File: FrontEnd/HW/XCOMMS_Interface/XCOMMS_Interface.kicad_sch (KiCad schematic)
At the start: 37 parts, among them J1 TFC-110-02-F-D-A-P-FR, J2 PicoBlade01x05, J3 PicoBlade01x05, J4 PicoBlade01x02, U1 STM32L051K8Tx, Y1 ECS-.327-7-34QCS-TR

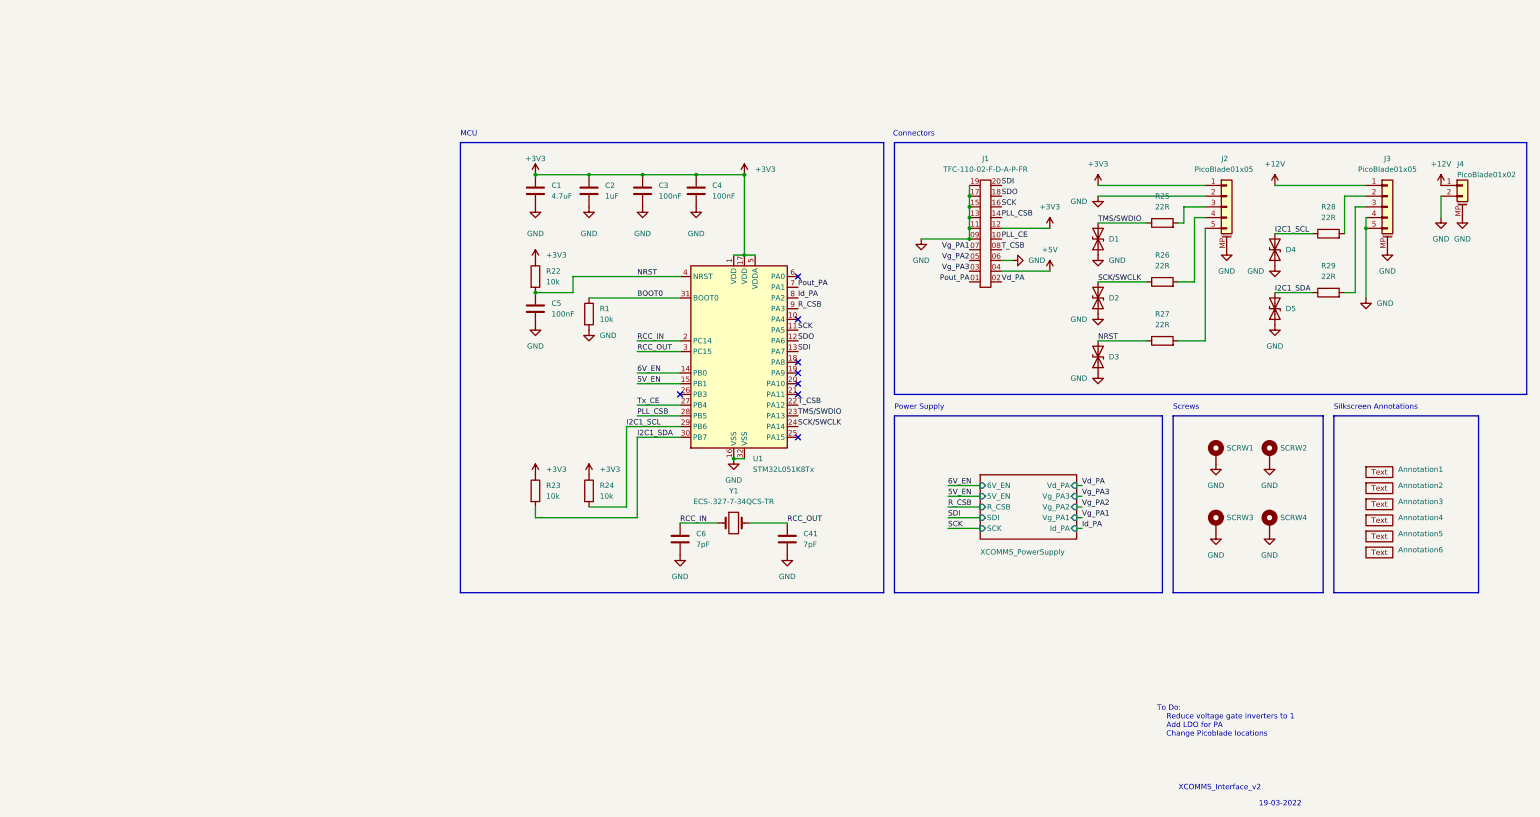
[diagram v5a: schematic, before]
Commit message: redundant MCU
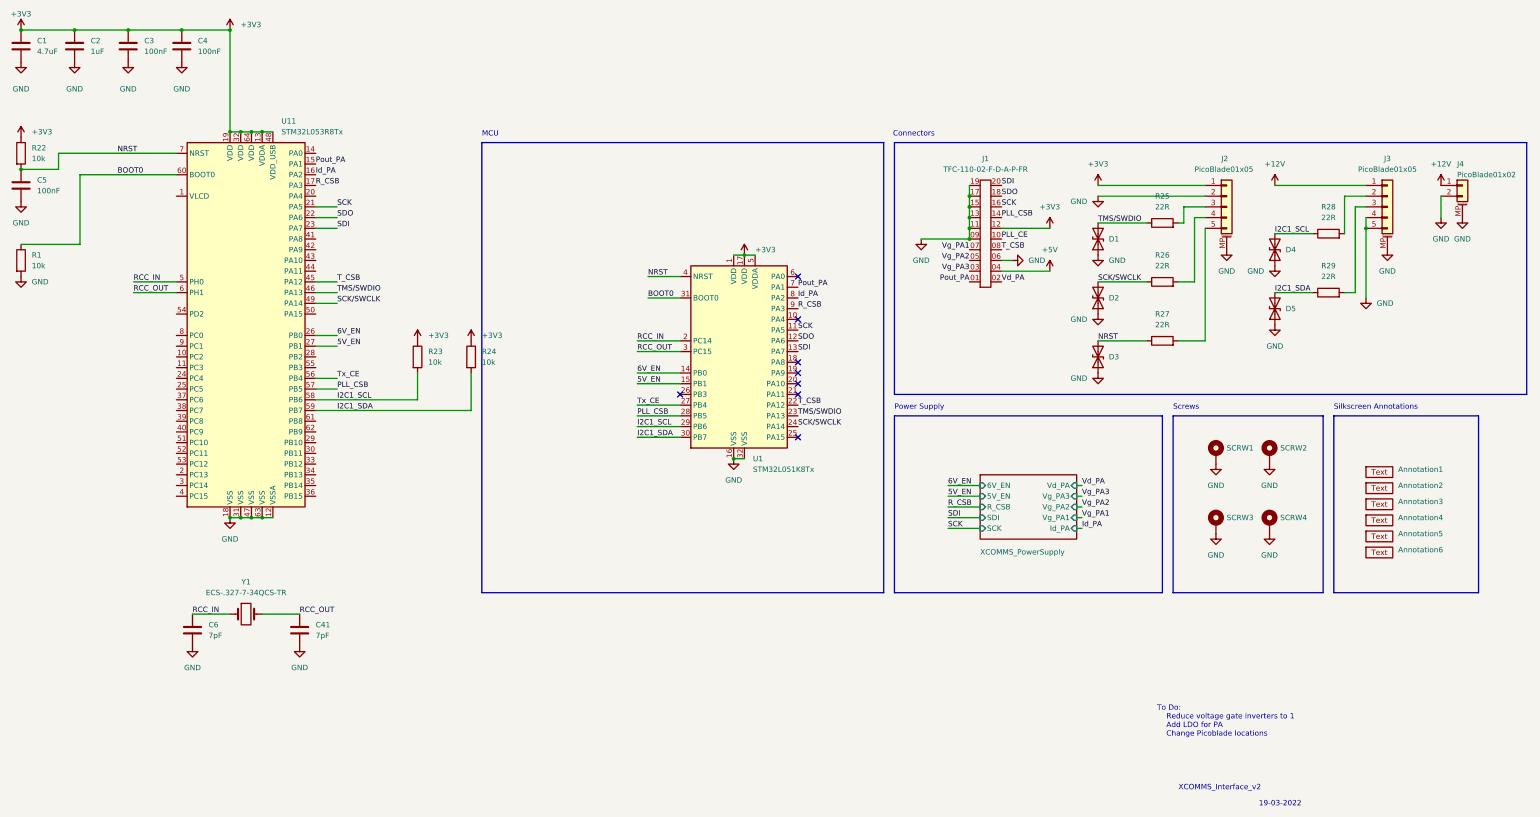
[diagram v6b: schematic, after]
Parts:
- added U11: STM32L053R8Tx, Package_QFP:LQFP-64_10x10mm_P0.5mm, symbol MCU_ST_STM32L0:STM32L053R8Tx
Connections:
- net +3V3: now also U11.13 (VDDA), U11.19 (VDD), U11.32 (VDD), U11.48 (VDD_USB), U11.64 (VDD)
- net 5V_EN: now also U11.27 (PB1)
- net 6V_EN: now also U11.26 (PB0)
- net BOOT0: now also U11.60 (BOOT0)
- net GND: now also U11.12 (VSSA), U11.18 (VSS), U11.31 (VSS), U11.47 (VSS), U11.63 (VSS)
- net I2C1_SCL: now also R23.2, U11.58 (PB6); no longer R24.2
- net I2C1_SDA: now also R24.2, U11.59 (PB7); no longer R23.2
- net Id_PA: now also U11.16 (PA2)
- net NRST: now also U11.7 (NRST)
- net PLL_CSB: now also U11.57 (PB5)
- net Pout_PA: now also U11.15 (PA1)
- net RCC_IN: now also U11.5 (PH0)
- net RCC_OUT: now also U11.6 (PH1)
- net R_CSB: now also U11.17 (PA3)
- net SCK: now also U11.21 (PA5)
- net SCK/SWCLK: now also U11.49 (PA14)
- net SDI: now also U11.23 (PA7)
- net SDO: now also U11.22 (PA6)
- net TMS/SWDIO: now also U11.46 (PA13)
- net T_CSB: now also U11.45 (PA12)
- net Tx_CE: now also U11.56 (PB4)
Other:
- moved on the sheet: C1, C2, C3, C4, C41, C5, C6, R1, R22, Y1

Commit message: starting redundant mcu
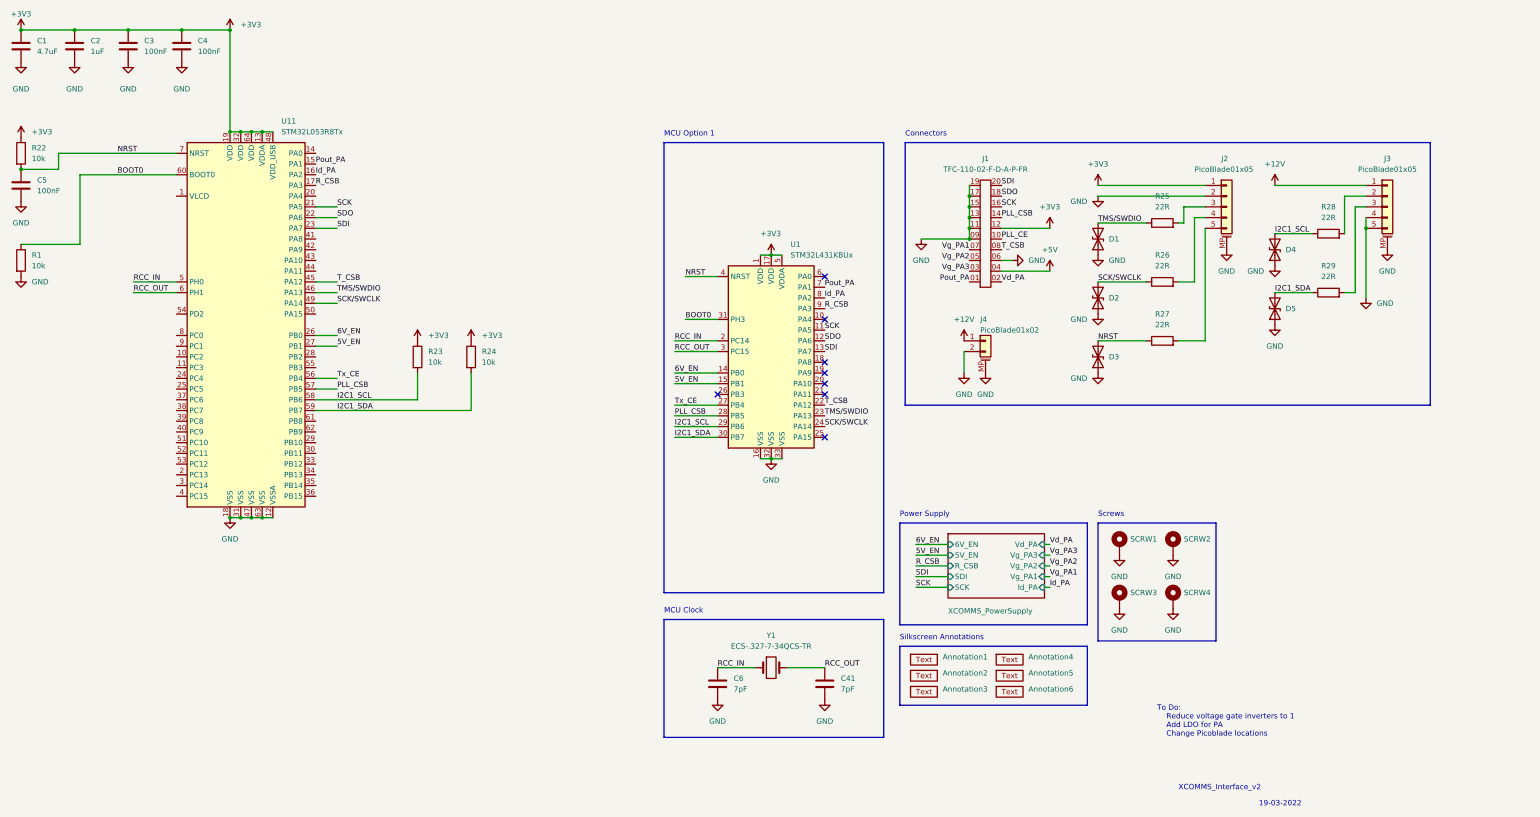
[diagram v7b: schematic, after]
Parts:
- removed U1: STM32L051K8Tx, Package_QFP:LQFP-32_7x7mm_P0.8mm, symbol MCU_ST_STM32L0:STM32L051K8Tx
- added U1: STM32L431KBUx, Package_DFN_QFN:QFN-32-1EP_5x5mm_P0.5mm_EP3.45x3.45mm, symbol MCU_ST_STM32L4:STM32L431KBUx
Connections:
- net +3V3: now also U1.1 (VDD), U1.17 (VDD), U1.5 (VDDA)
- net 5V_EN: now also U1.15 (PB1)
- net 6V_EN: now also U1.14 (PB0)
- net BOOT0: now also U1.31 (PH3)
- net GND: now also U1.16 (VSS), U1.32 (VSS), U1.33 (VSS)
- net I2C1_SCL: now also U1.29 (PB6)
- net I2C1_SDA: now also U1.30 (PB7)
- net Id_PA: now also U1.8 (PA2)
- net NRST: now also U1.4 (NRST)
- net PLL_CSB: now also U1.28 (PB5)
- net Pout_PA: now also U1.7 (PA1)
- net RCC_IN: now also U1.2 (PC14)
- net RCC_OUT: now also U1.3 (PC15)
- net R_CSB: now also U1.9 (PA3)
- net SCK: now also U1.11 (PA5)
- net SCK/SWCLK: now also U1.24 (PA14)
- net SDI: now also U1.13 (PA7)
- net SDO: now also U1.12 (PA6)
- net TMS/SWDIO: now also U1.23 (PA13)
- net T_CSB: now also U1.22 (PA12)
- net Tx_CE: now also U1.27 (PB4)
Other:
- note added: "MCU Clock"
- note added: "MCU Option 1"
- note removed: "MCU"
- moved on the sheet: Annotation1, Annotation2, Annotation3, Annotation4, Annotation5, Annotation6, C41, C6, J4, SCRW1, SCRW2, SCRW3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

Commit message: continuation of previous
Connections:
- net I2C1_SCL: now also U1.19 (PA9); no longer U1.29 (PB6)
- net I2C1_SDA: now also U1.20 (PA10); no longer U1.30 (PB7)
- net RCC_IN: no longer U1.2 (PC14)
- net RCC_OUT: no longer U1.3 (PC15)
- net R_CSB: now also U1.10 (PA4), U11.20 (PA4); no longer U1.9 (PA3), U11.17 (PA3)
- net RCC_IN_HSE: now reaches U1.6 (PA0)
- no-connect marks 8 -> 9
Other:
- moved on the sheet: C1, C2, C3, C4, R23, R24
